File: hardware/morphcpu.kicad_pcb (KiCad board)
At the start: 4 copper layers, 70 x 70 mm, 84 parts, among them J1 TYPE-C-31-M-12, SW1 TS-1187A-B-A-B, U1 ICE40UP5K-SG48I, U2 FT231XS-R, U3 W25Q32JVSSIQ, U4 ME6211C33M5G-N, U5 ME6211C12M5G-N, U6 USBLC6-2SC6, X1 1532H4-16000JWPDTSNL

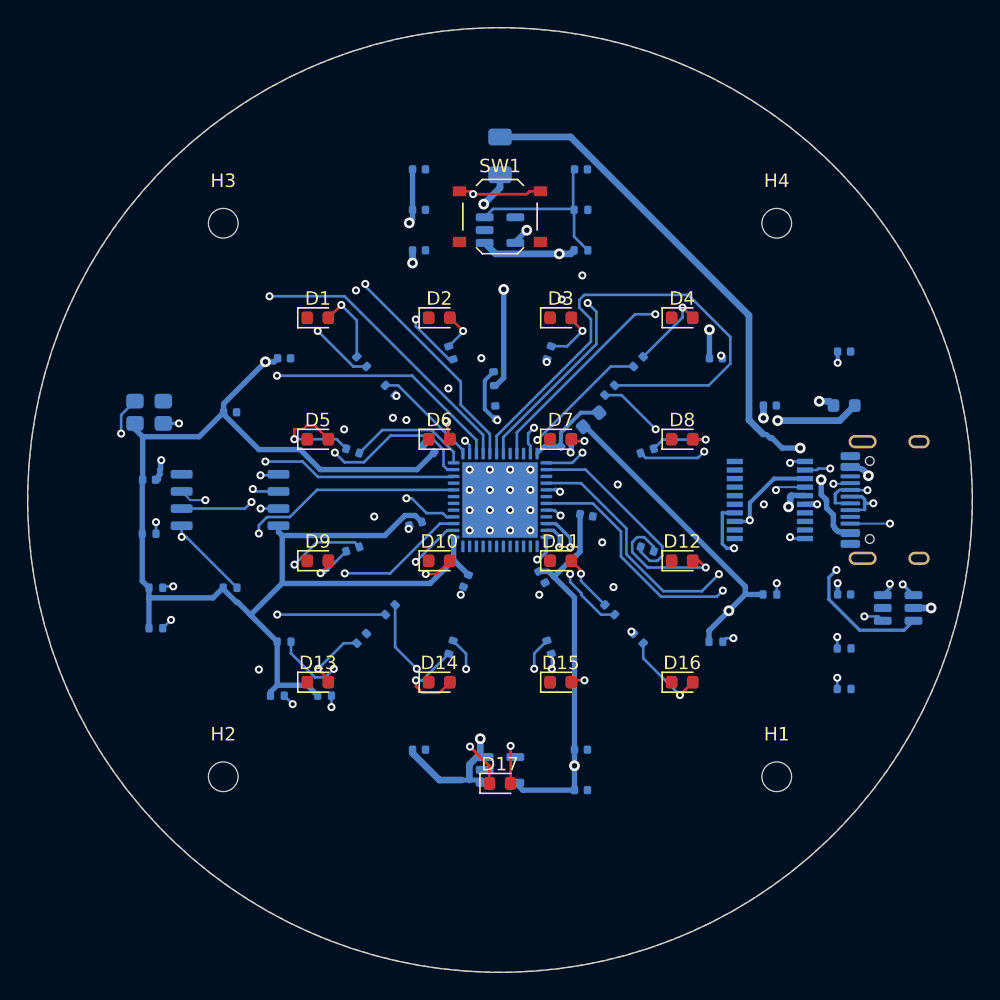
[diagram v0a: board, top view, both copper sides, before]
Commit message: fanout was full / six leds onto the south row
U1's east column was carrying twelve nets on twelve 0.5 mm channels and four of
them land on the far side of the board so they cross the fan twice. +3V3 at 22
and 33, +1V2 at 5 and 30, and LED12 had no escape at all

a 0.6 mm via wants 1.2 mm between its neighbours and adjacent escape rays are
0.5 mm apart, so nothing changes layer until the fan has spread. the staggered
two row via fanout fails the same way, the outer neck needs 1.2 mm between two
inner vias and has 1.0 mm. tested that

pads 37-48 were sitting unused. LED12 27->48, LED13 28->46, LED14 31->38,
LED2 4->23, LED3 11->27, ordered by their resistors x so none of them cross.
46/47/48 are bank 2 and 23/27/38 are bank 0, both already +3V3 so no level
change. nothing lands on a config pin, an RGB driver or a global buffer, 20 (G3)
stays free, CLK stays on 35. bank balance 15/30/35 mA -> 25/25/30

LED12/13/14 went 42.0 / 36.1 mm and unroutable to 12.5 / 7.8 / 8.0 mm and eleven
of the twelve outstanding connections then routed with nothing ripped up

four router bugs fixed on the way, each throwing away channels that were legal.
fill_poly rasterising cells as half open squares while cell()/pos() used lattice
points, 0.025 mm off. obstacles inflated by clearance + 0.01 mm when the tightest
real clearances here are 0.2019 mm against a 0.2 mm rule. hole to hole checks
reading ripped up vias off the board's original track list. a route's own vias
never checked against each other, two layer changes in neighbouring cells puts
two holes 0.07 mm apart

netlist.py, morphcpu.pcf and the DESIGN.md pin table moved together, ERC 0/0
after regenerating. VBUS_IN widened to its 0.5 mm class width. USB_DP/DM and
CC1/CC2 untouched, byte identical widths and lengths

0 violations, 7 unconnected -> 0 violations, 3 unconnected
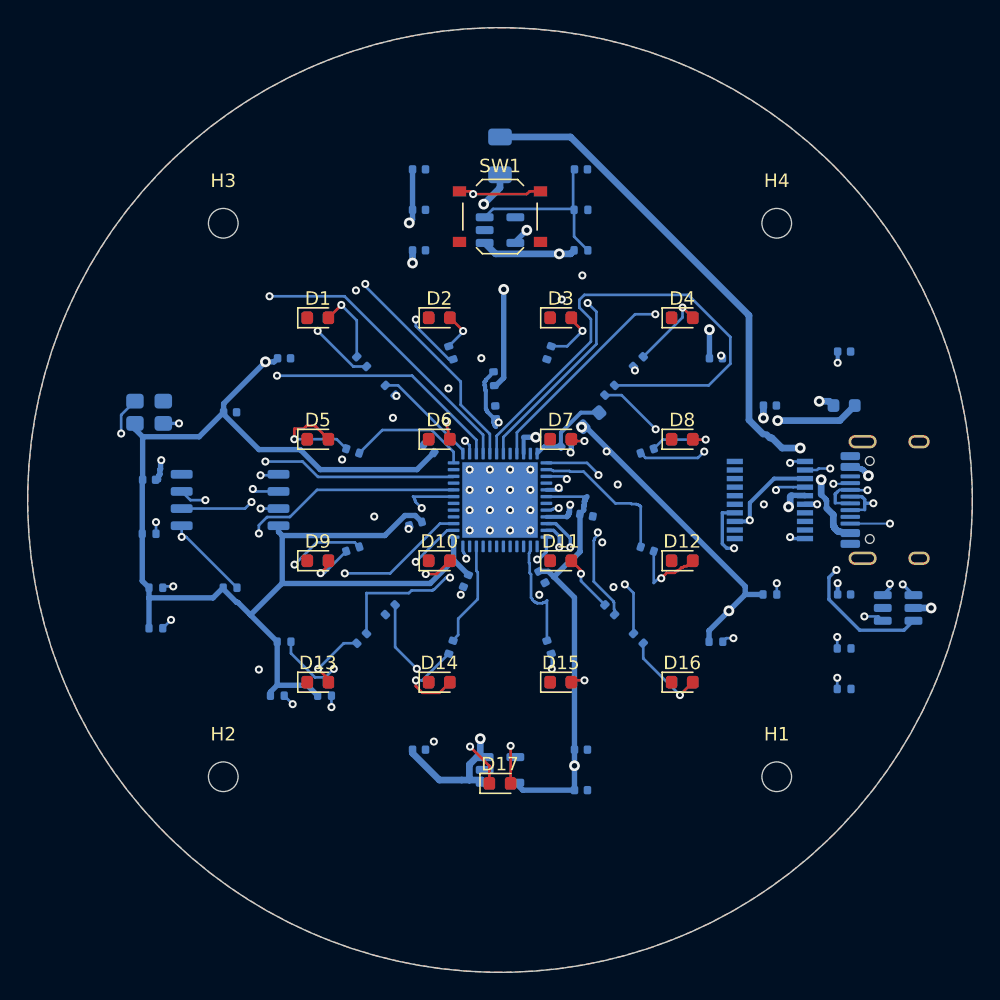
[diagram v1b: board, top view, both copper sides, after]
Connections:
- U1 pad 11: LED3 -> unconnected-(U1B-IOB_20a-Pad11)
- U1 pad 23: LED9 -> LED2
- U1 pad 27: LED12 -> LED3
- U1 pad 28: LED13 -> unconnected-(U1A-IOT_41a-Pad28)
- U1 pad 31: LED14 -> unconnected-(U1A-IOT_42b-Pad31)
- U1 pad 38: unconnected-(U1A-IOT_50b-Pad38) -> LED14
- U1 pad 4: LED2 -> unconnected-(U1C-IOB_8a-Pad4)
- U1 pad 46: unconnected-(U1C-IOB_0a-Pad46) -> LED13
- U1 pad 47: unconnected-(U1C-IOB_2a-Pad47) -> LED9
- U1 pad 48: unconnected-(U1C-IOB_4a-Pad48) -> LED12
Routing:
- net LED9: track 40.1 -> 0.00 mm, vias 3 -> 0
- net LED13: track 41.9 -> 7.47 mm, vias 2 -> 0
- net LED14: track 36.1 -> 7.96 mm, vias 2 -> 0
- net LED3: track 36.4 -> 11.9 mm
- net LED2: track 22.3 -> 0.00 mm, vias 3 -> 0
- net CDONE: track 18.7 -> 40.7 mm, vias 2 -> 4
- net +3V3: track 194.9 -> 208.3 mm, vias 5 -> 9
- net LED12: track 0.00 -> 12.2 mm, vias 0 -> 2
- net LED11_A: track 10.2 -> 5.39 mm
- net +1V2: track 72.8 -> 77.0 mm
- net LED10: track 18.5 -> 15.0 mm
- net LED11: track 14.0 -> 10.7 mm
- net VCCPLL_F: track 14.8 -> 12.9 mm
- net GND: vias 29 -> 30

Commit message: led9 onto pin 9 / +1V2 gets out of U1.5
LED9 went to the south row with LED12/13/14 last commit and then spent its time
fighting LED12 on pad 48 for the same southwest corridor. R10 is at 141.5, 108.5
and pad 9's ray on the west face points straight at it, so it goes there and pad
47 is unused again

that frees the west corridor and +1V2 at U1.5 routes. pin 5 is a core VCC pin so
it was the only open connection that actually mattered

left is LED1 (U1.3 -> R2.1) and LED2 (U1.23 -> R3.1). both route alone, never
together. seven pin assignments trialled with +1V2 placed first and every one
lands on two open, just a different two, table is in ROUTING.md

netlist.py, morphcpu.pcf and the DESIGN.md pin table moved together. ERC 0,
board and regenerated schematic agree on every unconnected U1 pad

0 violations, 3 unconnected -> 0 violations, 2 unconnected
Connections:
- U1 pad 47: LED9 -> unconnected-(U1C-IOB_2a-Pad47)
- U1 pad 9: unconnected-(U1B-IOB_16a-Pad9) -> LED9
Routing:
- net LED1: track 34.9 -> 0.00 mm, vias 2 -> 0
- net LED0: track 47.0 -> 16.6 mm
- net LED9: track 0.00 -> 29.9 mm, vias 0 -> 3
- net +1V2: track 77.0 -> 91.3 mm, vias 2 -> 4
- net CDONE: track 40.7 -> 38.5 mm
